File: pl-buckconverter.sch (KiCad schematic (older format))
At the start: 22 parts, among them J7 LOAD, Q10 MMBT2222A, Q11 PHD45N03LTA, Q12 PHD45N03LTA, Q9 MMBT2222A

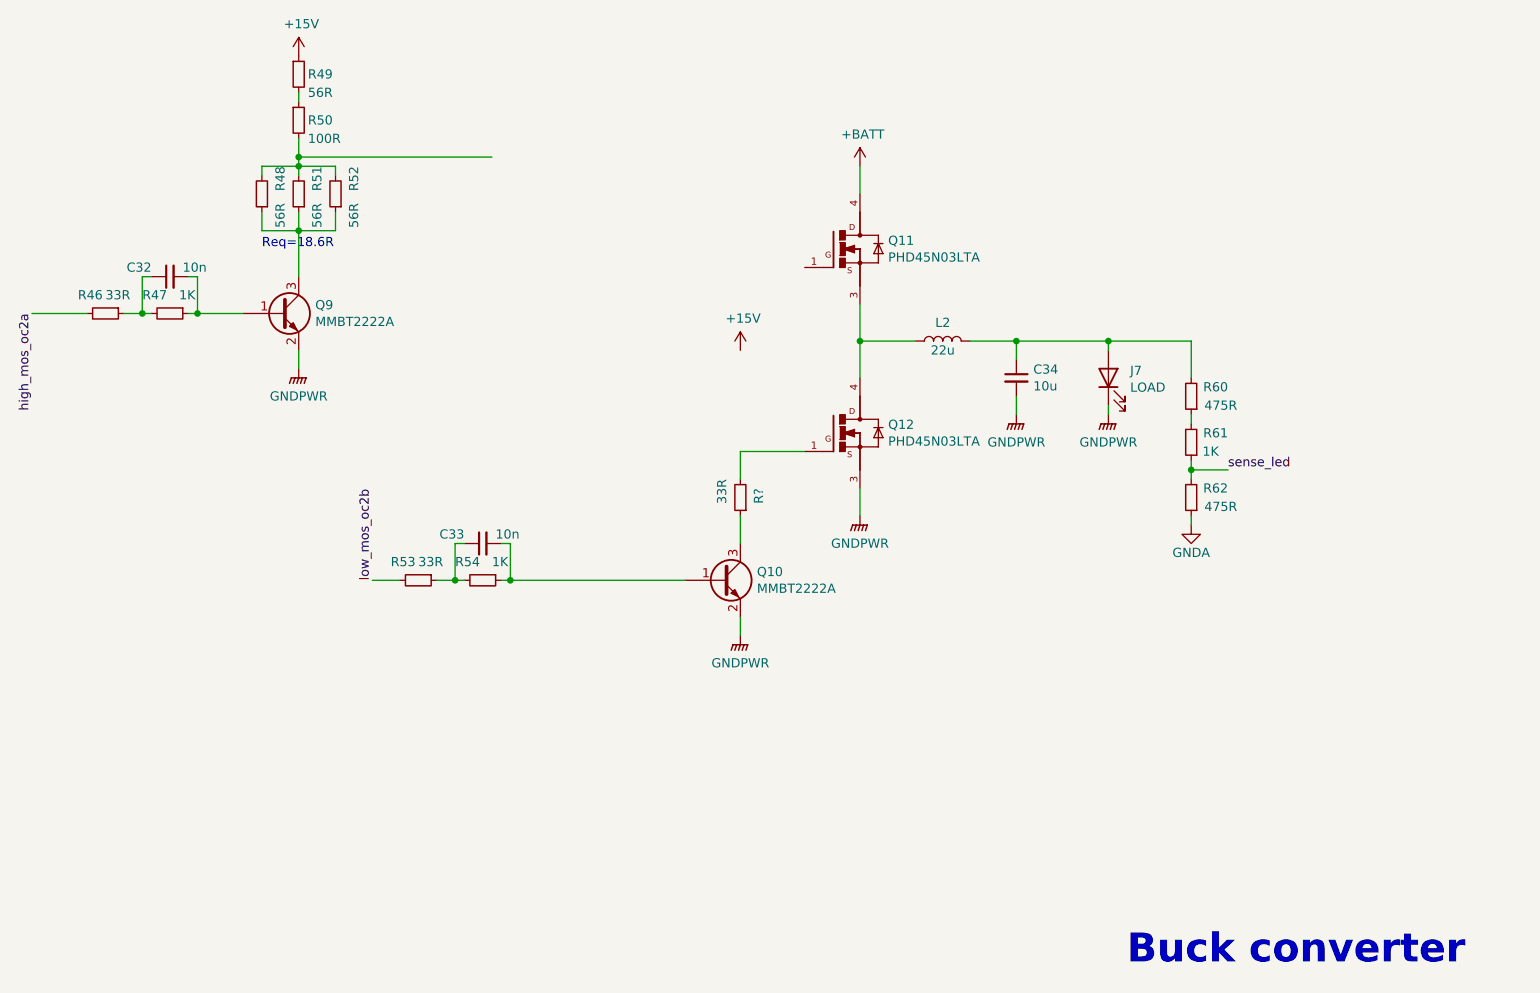
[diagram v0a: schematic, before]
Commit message: Fixed hierarchical sheet for microcontroller unit
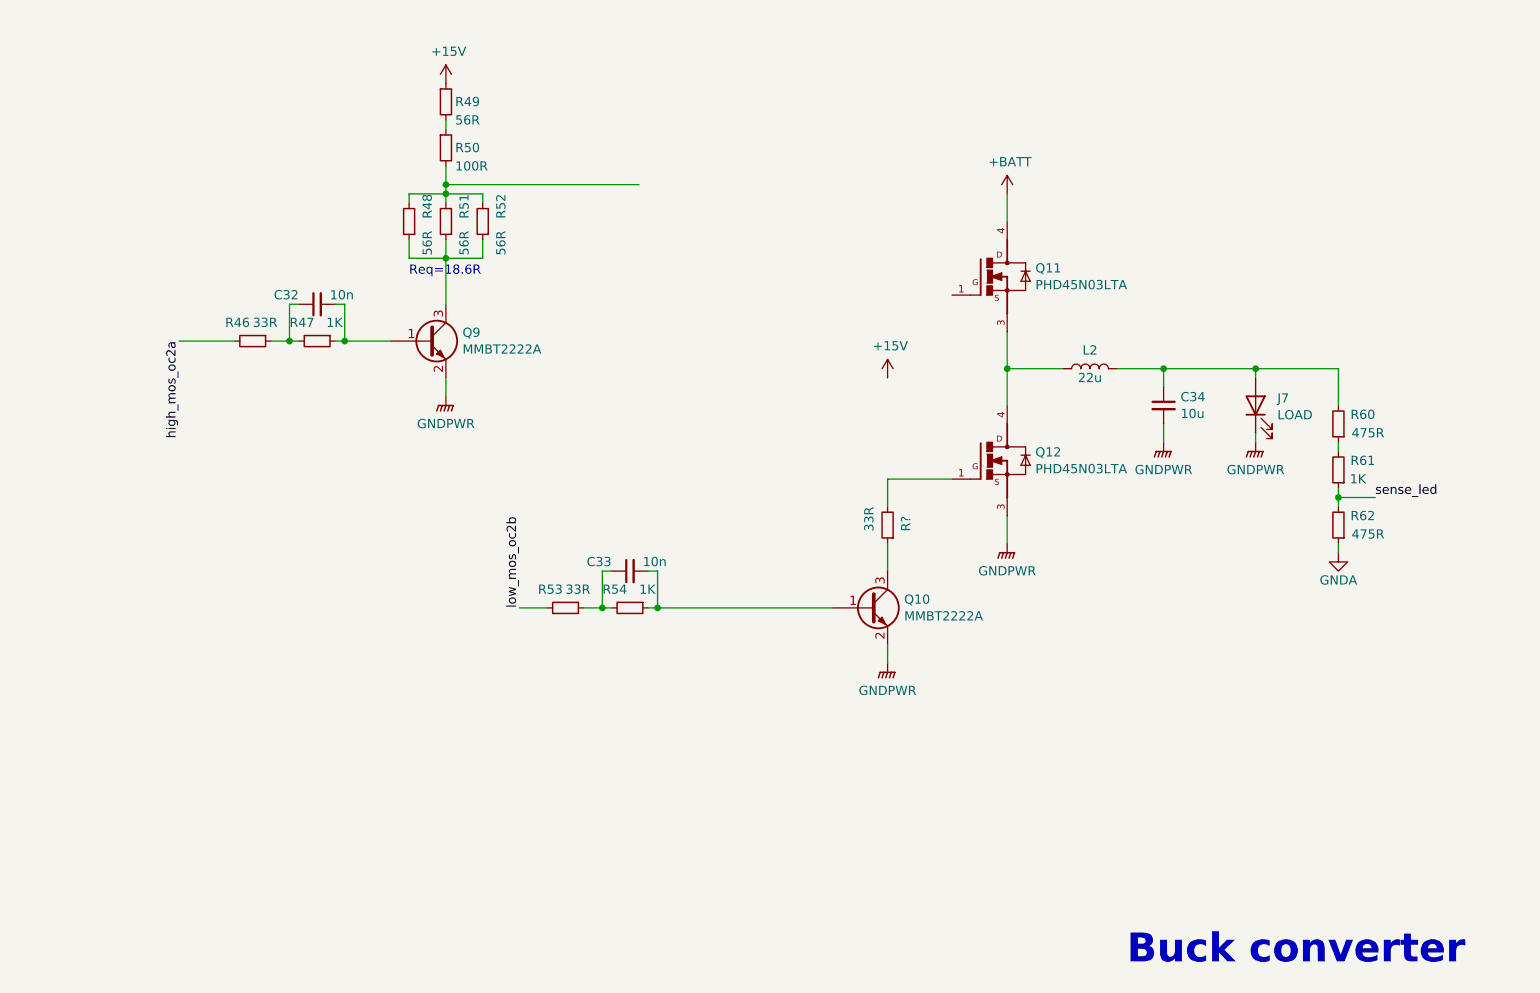
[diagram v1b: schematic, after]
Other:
- moved on the sheet: C32, C33, C34, J7, L2, Q10, Q11, Q12, Q9, R46, R47, R48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
